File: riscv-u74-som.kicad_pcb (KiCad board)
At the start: 2 copper layers, 55 x 40 mm, 13 parts, among them J1 DF40HC(3.0)-100DS-0.4v, J2 DF40HC(3.0)-100DS-0.4v, U1 SiFive-U74, U2 MT53E256M32D2, U3 MT53E256M32D2, U4 S25FL128SAGNFI000, U5 TPS65086100, U6 TDA19988BHN_C1,557, U7 KSZ9031RNXCA

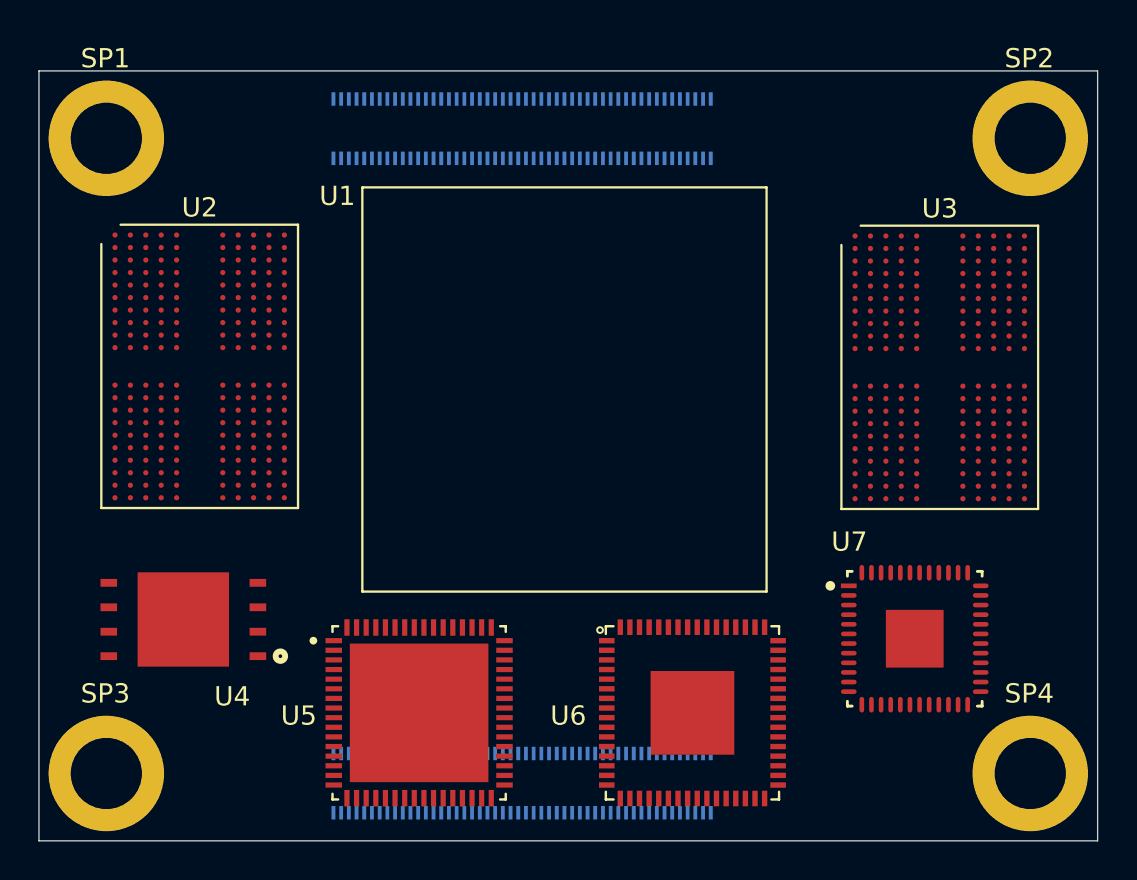
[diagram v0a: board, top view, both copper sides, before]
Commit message: Flipped standoffs in mock PCB
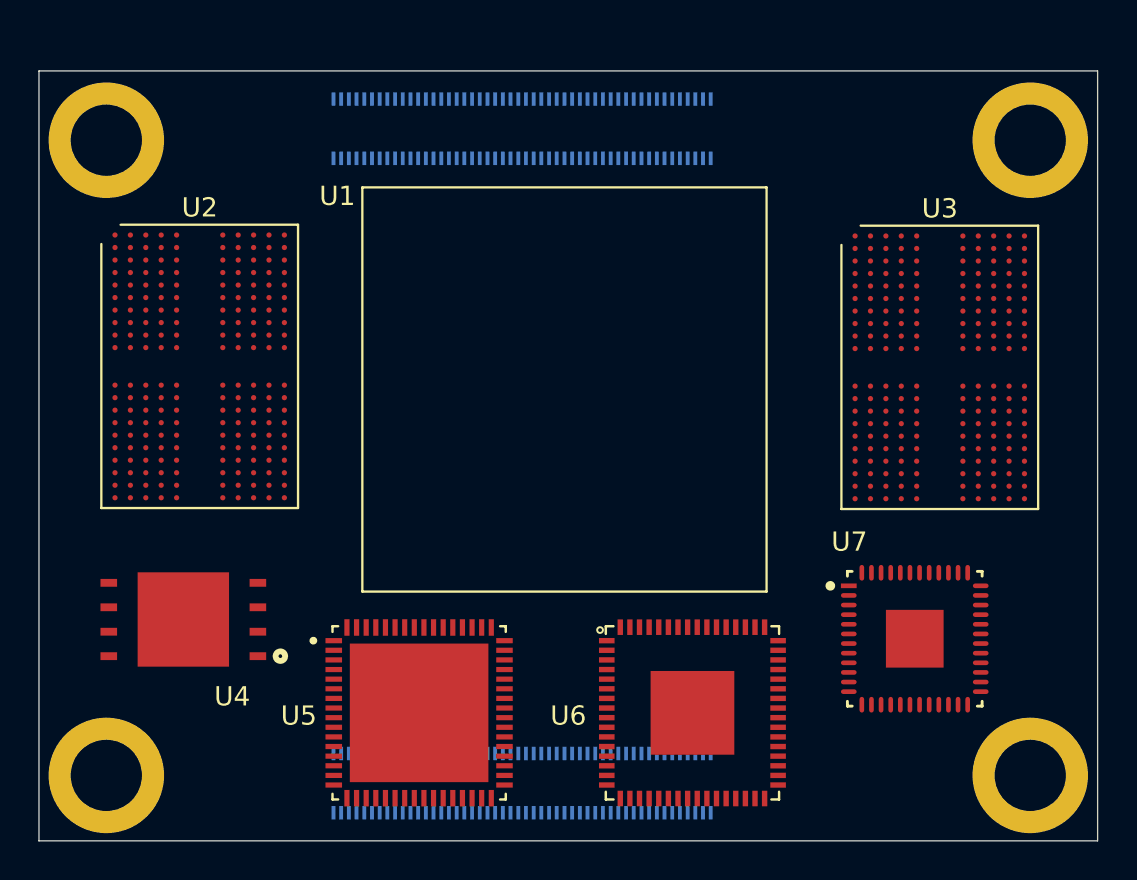
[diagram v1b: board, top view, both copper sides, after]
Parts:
- SP1, SP2, SP3, SP4: moved to B.Cu

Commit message: Updated mock
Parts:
- removed J1, J2: DF40HC(3.0)-100DS-0.4v, antmicro-footprints:DF40HC(3.0)-100DS-0.4v
- removed U1: SiFive-U74, antmicro-footprints:SiFive-U74
- removed U4: S25FL128SAGNFI000, antmicro-footprints:S25FL128SAGNFI000
- removed U5: TPS65086100, antmicro-footprints:QFN50P900X900X80-65N
- removed U6: TDA19988BHN_C1,557, antmicro-footprints:QFN50P900X900X100-65N
- removed U7: KSZ9031RNXCA, antmicro-footprints:QFN-48-Microchip-QFN77-48LD-PL-2
- added G***: LOGO, antmicro-footprints:antmicro-logo_scaled_15mm, F.Cu at (147.9, 58.2)
- added J3: DF40C-100DP-0.4V(51), antmicro-footprints:HRS_DF40C-100DP-0.4V(51), B.Cu at (155.1, 58.0)
- added J4: DF40C-100DP-0.4V(51), antmicro-footprints:HRS_DF40C-100DP-0.4V(51), B.Cu at (155.1, 92.0)
- added U10: TDA19988BHN_C1,557, antmicro-footprints:QFN50P900X900X100-65N, F.Cu at (164.0, 88.3)
- added U11: KSZ9031RNXCA, antmicro-footprints:QFN-48-Microchip-QFN77-48LD-PL-2, F.Cu at (173.0, 60.5)
- added U13: VIC7100, antmicro-footprints:vic7100, F.Cu at (145.3, 61.9)
- added U8: TPS65086100, antmicro-footprints:QFN50P900X900X80-65N, F.Cu at (146.8, 88.3)
- added U9: GD25LQ256DWIGR, antmicro-footprints:8-WSON-6x5, F.Cu at (177.0, 86.0)
- SP1, SP2, SP3, SP4: footprint antmicro-footprints:9774030151 -> riscv-u74-som-footprints:9774030151
- U2, U3: footprint antmicro-footprints:BGA-200_10.0x14.5mm_Layout12x22_P0.80x0.65mm -> riscv-u74-som-footprints:BGA-200_10.0x14.5mm_Layout12x22_P0.80x0.65mm
- moved U2 3.81 mm to (136.9, 73.8)
- moved U3 3.81 mm to (175.3, 73.9)
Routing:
- net (no net): track 0.00 -> 225.1 mm, vias 0 -> 20
- net Net-(U2-PadA10): track 0.00 -> 25.6 mm
- net GND: track 0.00 -> 19.7 mm, vias 0 -> 4
- net Net-(U3-PadAB10): track 0.00 -> 9.79 mm, vias 0 -> 1
- net Net-(U2-PadC11): track 0.00 -> 9.35 mm
- net Net-(U3-PadAA1): track 0.00 -> 9.35 mm
- net Net-(U2-PadA4): track 0.00 -> 8.92 mm
- net Net-(U13-PadAF1): track 0.00 -> 8.92 mm
- net USB_SSTXA2: track 0.00 -> 8.92 mm
- net RPI_GPIO8: track 0.00 -> 8.88 mm
- net DDR1_DQ05: track 0.00 -> 8.88 mm
- net RPI_GPIO20: track 0.00 -> 7.87 mm
- net DDR1_DQ02: track 0.00 -> 7.87 mm
- net CSI1RX_CLK_P: track 0.00 -> 7.15 mm
- net Net-(U13-PadAG1): track 0.00 -> 7.15 mm
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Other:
- net class Default: clearance 0.2 -> 0.1; trace_width 0.25 -> 0.11
- rule trace_clearance: 0.2 -> 0.1
- rule trace_min: 0.2 -> 0.11
- board text added: "ARV"
- board text added: "Rev. 1.0.0 04/2021"

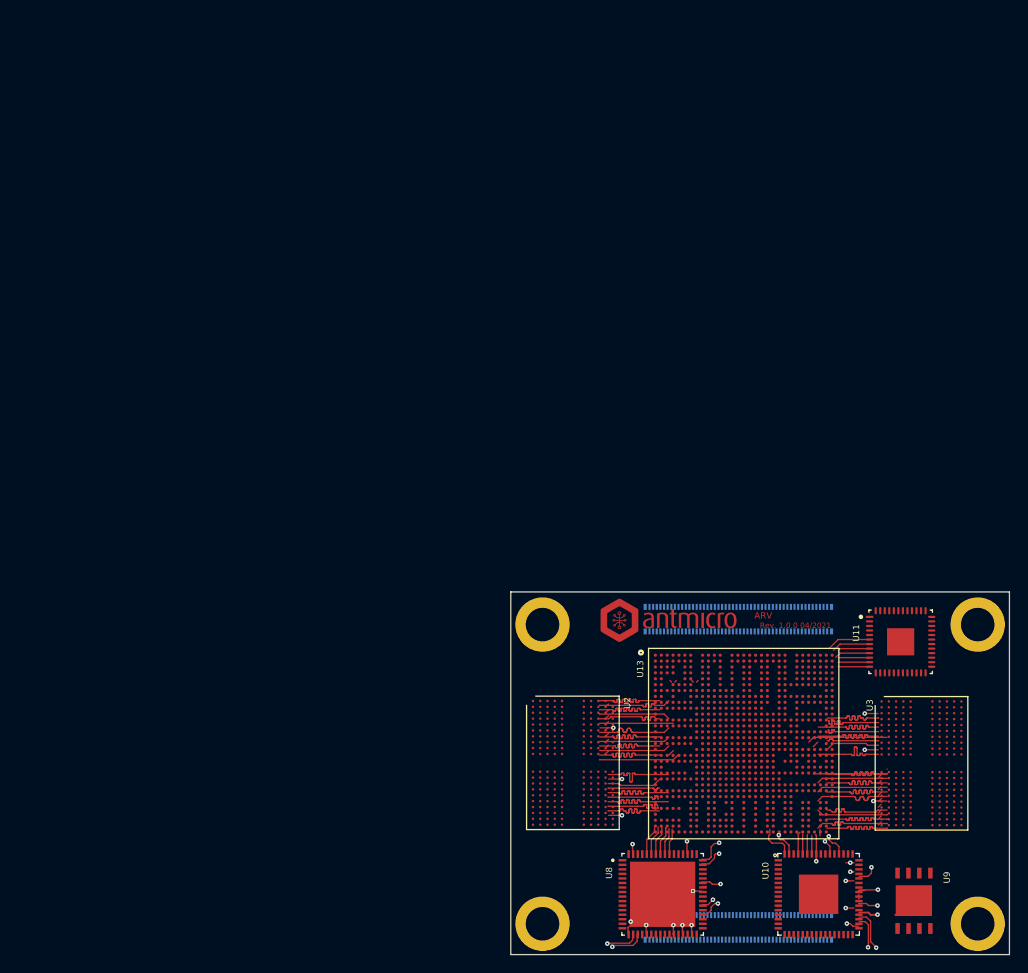
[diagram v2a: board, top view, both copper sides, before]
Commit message: Connected interfaces to VIC to visualise its ball locations (wip, mock purposes)
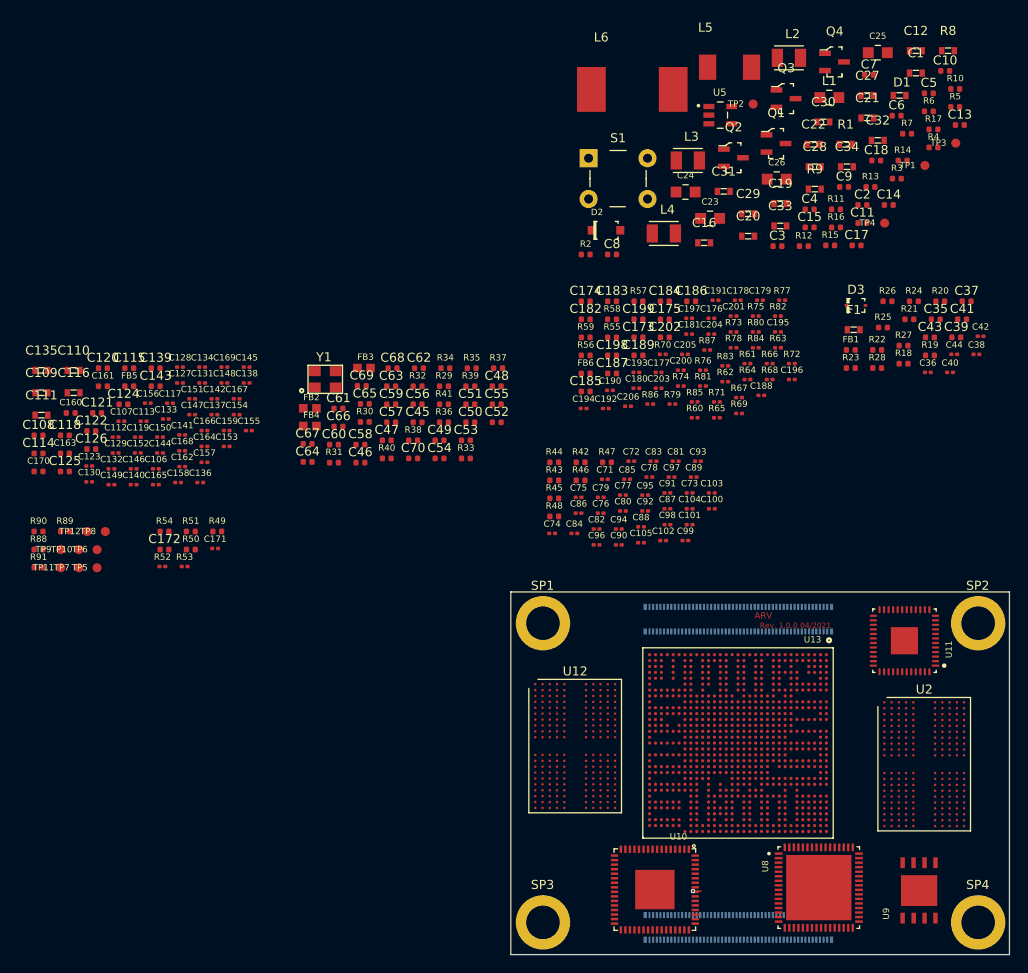
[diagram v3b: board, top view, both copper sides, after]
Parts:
- removed G***: LOGO, antmicro-footprints:antmicro-logo_scaled_15mm
- removed U3: MT53E256M32D2, riscv-u74-som-footprints:BGA-200_10.0x14.5mm_Layout12x22_P0.80x0.65mm
- added C1: C_10u_0603, antmicro-footprints:0603-cap, F.Cu at (174.7, -2.26)
- added C10: C_100n_0402_16V, antmicro-footprints:0402-cap, F.Cu at (177.9, -2.50)
- added C100: C_100n_0201, antmicro-footprints:0201-res, F.Cu at (152.2, 45.8)
- added C101: C_100n_0201, antmicro-footprints:0201-res, F.Cu at (149.7, 47.6)
- added C102: C_100n_0201, antmicro-footprints:0201-res, F.Cu at (146.8, 49.3)
- added C103: C_100n_0201, antmicro-footprints:0201-res, F.Cu at (152.2, 44.1)
- added C104: C_100n_0201, antmicro-footprints:0201-res, F.Cu at (149.7, 45.8)
- added C105: C_100n_0201, antmicro-footprints:0201-res, F.Cu at (144.4, 49.5)
- added C106: C_100n_0201, antmicro-footprints:0201-res, F.Cu at (90.9, 41.4)
- added C107: C_100n_0201, antmicro-footprints:0201-res, F.Cu at (87.1, 36.1)
- added C108: C_1u_0402, antmicro-footprints:0402-cap, F.Cu at (77.9, 37.7)
- added C109: C_22u_0603, antmicro-footprints:0603-cap, F.Cu at (78.3, 33.0)
- added C11: C_4u7_0402, antmicro-footprints:0402-cap, F.Cu at (168.8, 14.3)
- added C110: C_22u_0603, antmicro-footprints:0603-cap, F.Cu at (81.8, 30.5)
- added C111: C_22u_0603, antmicro-footprints:0603-cap, F.Cu at (78.3, 35.5)
- added C112: C_100n_0201, antmicro-footprints:0201-res, F.Cu at (86.4, 37.9)
- added C113: C_100n_0201, antmicro-footprints:0201-res, F.Cu at (89.5, 36.1)
- added C114: C_10u_0402, antmicro-footprints:0402-cap, F.Cu at (77.9, 39.7)
- added C115: C_10u_0402, antmicro-footprints:0402-cap, F.Cu at (87.9, 30.3)
- added C116: C_22u_0603, antmicro-footprints:0603-cap, F.Cu at (81.8, 33.0)
- added C117: C_100n_0201, antmicro-footprints:0201-res, F.Cu at (92.4, 34.2)
- added C118: C_10u_0402, antmicro-footprints:0402-cap, F.Cu at (80.8, 37.7)
- added C119: C_100n_0201, antmicro-footprints:0201-res, F.Cu at (88.9, 37.9)
- added C12: C_1n_0603, antmicro-footprints:0603-cap, F.Cu at (174.7, -4.73)
- added C120: C_10u_0402, antmicro-footprints:0402-cap, F.Cu at (85.0, 30.3)
- added C121: C_10u_0402, antmicro-footprints:0402-cap, F.Cu at (84.4, 35.2)
- added C122: C_10u_0402, antmicro-footprints:0402-cap, F.Cu at (83.8, 37.2)
- added C123: C_100n_0201, antmicro-footprints:0201-res, F.Cu at (83.5, 41.1)
- added C124: C_1u_0402, antmicro-footprints:0402-cap, F.Cu at (87.3, 34.3)
- added C125: C_1u_0402, antmicro-footprints:0402-cap, F.Cu at (80.8, 41.7)
- added C126: C_1u_0402, antmicro-footprints:0402-cap, F.Cu at (83.8, 39.2)
- added C127: C_100n_0201, antmicro-footprints:0201-res, F.Cu at (93.5, 31.9)
- added C128: C_100n_0201, antmicro-footprints:0201-res, F.Cu at (93.5, 30.2)
- added C129: C_100n_0201, antmicro-footprints:0201-res, F.Cu at (86.4, 39.6)
- added C13: C_100n_0402_16V, antmicro-footprints:0402-cap, F.Cu at (179.6, 3.47)
- added C130: C_100n_0201, antmicro-footprints:0201-res, F.Cu at (83.5, 42.8)
- added C131: C_100n_0201, antmicro-footprints:0201-res, F.Cu at (96.0, 31.9)
- added C132: C_100n_0201, antmicro-footprints:0201-res, F.Cu at (86.0, 41.4)
- added C133: C_100n_0201, antmicro-footprints:0201-res, F.Cu at (92.0, 35.9)
- added C134: C_100n_0201, antmicro-footprints:0201-res, F.Cu at (96.0, 30.2)
- added C135: C_22u_0603, antmicro-footprints:0603-cap, F.Cu at (78.3, 30.5)
- added C136: C_100n_0201, antmicro-footprints:0201-res, F.Cu at (95.8, 42.9)
- added C137: C_100n_0201, antmicro-footprints:0201-res, F.Cu at (97.3, 35.4)
- added C138: C_100n_0201, antmicro-footprints:0201-res, F.Cu at (100.9, 31.9)
- added C139: C_10u_0402, antmicro-footprints:0402-cap, F.Cu at (90.9, 30.3)
- added C14: C_4u7_0402, antmicro-footprints:0402-cap, F.Cu at (171.7, 12.3)
- added C140: C_100n_0201, antmicro-footprints:0201-res, F.Cu at (88.4, 43.1)
- added C141: C_100n_0201, antmicro-footprints:0201-res, F.Cu at (93.8, 37.7)
- added C142: C_100n_0201, antmicro-footprints:0201-res, F.Cu at (97.3, 33.7)
- added C143: C_1u_0402, antmicro-footprints:0402-cap, F.Cu at (90.9, 32.3)
- added C144: C_100n_0201, antmicro-footprints:0201-res, F.Cu at (91.3, 39.6)
- added C145: C_100n_0201, antmicro-footprints:0201-res, F.Cu at (100.9, 30.2)
- added C146: C_100n_0201, antmicro-footprints:0201-res, F.Cu at (88.4, 41.4)
- added C147: C_100n_0201, antmicro-footprints:0201-res, F.Cu at (94.9, 35.4)
- added C148: C_100n_0201, antmicro-footprints:0201-res, F.Cu at (98.4, 31.9)
- added C149: C_100n_0201, antmicro-footprints:0201-res, F.Cu at (86.0, 43.1)
- added C15: C_2u2_0402, antmicro-footprints:0402-cap, F.Cu at (163.0, 14.8)
- added C150: C_100n_0201, antmicro-footprints:0201-res, F.Cu at (91.3, 37.9)
- added C151: C_100n_0201, antmicro-footprints:0201-res, F.Cu at (94.9, 33.7)
- added C152: C_100n_0201, antmicro-footprints:0201-res, F.Cu at (88.9, 39.6)
- added C153: C_100n_0201, antmicro-footprints:0201-res, F.Cu at (98.7, 38.9)
- added C154: C_100n_0201, antmicro-footprints:0201-res, F.Cu at (99.8, 35.4)
- added C155: C_100n_0201, antmicro-footprints:0201-res, F.Cu at (101.1, 37.2)
- added C156: C_100n_0201, antmicro-footprints:0201-res, F.Cu at (90.0, 34.2)
- added C157: C_100n_0201, antmicro-footprints:0201-res, F.Cu at (96.2, 40.7)
- added C158: C_100n_0201, antmicro-footprints:0201-res, F.Cu at (93.3, 42.9)
- added C159: C_100n_0201, antmicro-footprints:0201-res, F.Cu at (98.7, 37.2)
- added C16: C_10u_0603, antmicro-footprints:0603-cap, F.Cu at (151.4, 16.5)
- added C160: C_1n_0402, antmicro-footprints:0402-res, F.Cu at (81.5, 35.2)
- added C161: C_1n_0402, antmicro-footprints:0402-res, F.Cu at (85.0, 32.3)
- added C162: C_100n_0201, antmicro-footprints:0201-res, F.Cu at (93.8, 41.2)
- added C163: C_1n_0402, antmicro-footprints:0402-res, F.Cu at (80.8, 39.7)
- added C164: C_100n_0201, antmicro-footprints:0201-res, F.Cu at (96.2, 38.9)
- added C165: C_100n_0201, antmicro-footprints:0201-res, F.Cu at (90.9, 43.1)
- added C166: C_100n_0201, antmicro-footprints:0201-res, F.Cu at (96.2, 37.2)
- added C167: C_100n_0201, antmicro-footprints:0201-res, F.Cu at (99.8, 33.7)
- added C168: C_100n_0201, antmicro-footprints:0201-res, F.Cu at (93.8, 39.4)
- added C169: C_100n_0201, antmicro-footprints:0201-res, F.Cu at (98.4, 30.2)
- added C17: C_100n_0402_16V, antmicro-footprints:0402-cap, F.Cu at (168.2, 16.8)
- added C170: C_1n_0402, antmicro-footprints:0402-res, F.Cu at (77.9, 41.7)
- added C171: C_100n_0201, antmicro-footprints:0201-res, F.Cu at (97.4, 50.2)
- added C172: C_10n_0402, antmicro-footprints:0402-cap, F.Cu at (91.8, 50.3)
- added C173: C_1u_0402, antmicro-footprints:0402-cap, F.Cu at (144.1, 26.9)
- added C174: C_1u_0402, antmicro-footprints:0402-cap, F.Cu at (138.3, 22.9)
- added C175: C_1u_0402, antmicro-footprints:0402-cap, F.Cu at (147.0, 24.9)
- added C176: C_100n_0201, antmicro-footprints:0201-res, F.Cu at (152.1, 24.8)
- added C177: C_100n_0201, antmicro-footprints:0201-res, F.Cu at (146.3, 30.8)
- added C178: C_100n_0201, antmicro-footprints:0201-res, F.Cu at (155.1, 22.8)
- added C179: C_100n_0201, antmicro-footprints:0201-res, F.Cu at (157.5, 22.8)
- added C18: C_100n_0402_16V, antmicro-footprints:0402-cap, F.Cu at (170.3, 7.39)
- added C180: C_100n_0201, antmicro-footprints:0201-res, F.Cu at (143.9, 32.5)
- added C181: C_100n_0201, antmicro-footprints:0201-res, F.Cu at (149.7, 26.5)
- added C182: C_10u_0402, antmicro-footprints:0402-cap, F.Cu at (138.3, 24.9)
- added C183: C_1u_0402, antmicro-footprints:0402-cap, F.Cu at (141.2, 22.9)
- added C184: C_10u_0402, antmicro-footprints:0402-cap, F.Cu at (147.0, 22.9)
- added C185: C_1u_0402, antmicro-footprints:0402-cap, F.Cu at (138.3, 32.9)
- added C186: C_1u_0402, antmicro-footprints:0402-cap, F.Cu at (149.9, 22.9)
- added C187: C_1u_0402, antmicro-footprints:0402-cap, F.Cu at (141.2, 30.9)
- added C188: C_100n_0201, antmicro-footprints:0201-res, F.Cu at (157.7, 33.3)
- added C189: C_1u_0402, antmicro-footprints:0402-cap, F.Cu at (144.1, 28.9)
- added C19: C_22u_0603, antmicro-footprints:0603-cap, F.Cu at (159.8, 12.1)
- added C190: C_100n_0201, antmicro-footprints:0201-res, F.Cu at (141.0, 32.7)
- added C191: C_100n_0201, antmicro-footprints:0201-res, F.Cu at (152.6, 22.8)
- added C192: C_100n_0201, antmicro-footprints:0201-res, F.Cu at (140.5, 34.7)
- added C193: C_100n_0201, antmicro-footprints:0201-res, F.Cu at (143.9, 30.8)
- added C194: C_100n_0201, antmicro-footprints:0201-res, F.Cu at (138.1, 34.7)
- added C195: C_100n_0201, antmicro-footprints:0201-res, F.Cu at (159.5, 26.3)
- added C196: C_100n_0201, antmicro-footprints:0201-res, F.Cu at (161.0, 31.5)
- added C197: C_100n_0201, antmicro-footprints:0201-res, F.Cu at (149.7, 24.8)
- added C198: C_1u_0402, antmicro-footprints:0402-cap, F.Cu at (141.2, 28.9)
- added C199: C_1u_0402, antmicro-footprints:0402-cap, F.Cu at (144.1, 24.9)
- added C2: C_2u2_0402, antmicro-footprints:0402-cap, F.Cu at (168.8, 12.3)
- added C20: C_22u_0603, antmicro-footprints:0603-cap, F.Cu at (156.2, 15.7)
- added C200: C_100n_0201, antmicro-footprints:0201-res, F.Cu at (148.8, 30.5)
- added C201: C_100n_0201, antmicro-footprints:0201-res, F.Cu at (154.6, 24.5)
- added C202: C_1u_0402, antmicro-footprints:0402-cap, F.Cu at (147.0, 26.9)
- added C203: C_100n_0201, antmicro-footprints:0201-res, F.Cu at (146.3, 32.5)
- added C204: C_100n_0201, antmicro-footprints:0201-res, F.Cu at (152.1, 26.5)
- added C205: C_100n_0201, antmicro-footprints:0201-res, F.Cu at (149.2, 28.8)
- added C206: C_100n_0201, antmicro-footprints:0201-res, F.Cu at (143.0, 34.5)
- added C21: C_22u_0603, antmicro-footprints:0603-cap, F.Cu at (169.4, 2.69)
- added C22: C_22u_0603, antmicro-footprints:0603-cap, F.Cu at (163.4, 5.60)
- added C23: C_100u_0805, antmicro-footprints:0805-cap, F.Cu at (152.0, 13.8)
- added C24: C_100u_0805, antmicro-footprints:0805-cap, F.Cu at (149.3, 10.9)
- added C25: C_100u_0805, antmicro-footprints:0805-cap, F.Cu at (170.5, -4.51)
- added C26: C_100u_0805, antmicro-footprints:0805-cap, F.Cu at (159.4, 9.44)
- added C27: C_10u_0603, antmicro-footprints:0603-cap, F.Cu at (169.4, 0.22)
- added C28: C_10u_0603, antmicro-footprints:0603-cap, F.Cu at (163.6, 8.07)
- added C29: C_22u_0603, antmicro-footprints:0603-cap, F.Cu at (156.2, 13.3)
- added C3: C_2u2_0402, antmicro-footprints:0402-cap, F.Cu at (159.4, 16.8)
- added C30: C_22u_0603, antmicro-footprints:0603-cap, F.Cu at (164.5, 3.13)
- added C31: C_22u_0603, antmicro-footprints:0603-cap, F.Cu at (153.5, 10.8)
- added C32: C_22u_0603, antmicro-footprints:0603-cap, F.Cu at (170.5, 5.16)
- added C33: C_22u_0603, antmicro-footprints:0603-cap, F.Cu at (159.8, 14.6)
- added C34: C_22u_0603, antmicro-footprints:0603-cap, F.Cu at (167.1, 8.07)
- added C35: C_1u_0402, antmicro-footprints:0402-cap, F.Cu at (176.9, 24.9)
- added C36: C_100n_0201, antmicro-footprints:0201-res, F.Cu at (176.0, 30.8)
- added C37: C_2u2_0402, antmicro-footprints:0402-cap, F.Cu at (180.3, 22.9)
- added C38: C_100n_0201, antmicro-footprints:0201-res, F.Cu at (181.4, 28.8)
- added C39: C_2u2_0402, antmicro-footprints:0402-cap, F.Cu at (179.2, 26.9)
- added C4: C_2u2_0402, antmicro-footprints:0402-cap, F.Cu at (163.0, 12.8)
- added C40: C_100n_0201, antmicro-footprints:0201-res, F.Cu at (178.5, 30.8)
- added C41: C_2u2_0402, antmicro-footprints:0402-cap, F.Cu at (179.8, 24.9)
- added C42: C_100n_0201, antmicro-footprints:0201-res, F.Cu at (181.8, 26.8)
- added C43: C_2u2_0402, antmicro-footprints:0402-cap, F.Cu at (176.3, 26.9)
- added C44: C_100n_0201, antmicro-footprints:0201-res, F.Cu at (178.9, 28.8)
- added C45: C_4u7_0402, antmicro-footprints:0402-cap, F.Cu at (119.7, 36.3)
- added C46: C_470n_0402, antmicro-footprints:0402-cap, F.Cu at (113.4, 40.7)
- added C47: C_4u7_0402, antmicro-footprints:0402-cap, F.Cu at (116.3, 38.3)
- added C48: C_470n_0402, antmicro-footprints:0402-cap, F.Cu at (128.5, 32.3)
- added C49: C_4u7_0402, antmicro-footprints:0402-cap, F.Cu at (122.2, 38.3)
- added C5: C_2u2_0402, antmicro-footprints:0402-cap, F.Cu at (176.1, -0.03)
- added C50: C_4u7_0402, antmicro-footprints:0402-cap, F.Cu at (125.6, 36.3)
- added C51: C_470n_0402, antmicro-footprints:0402-cap, F.Cu at (125.6, 34.3)
- added C52: C_470n_0402, antmicro-footprints:0402-cap, F.Cu at (128.5, 36.3)
- added C53: C_470n_0402, antmicro-footprints:0402-cap, F.Cu at (125.1, 38.3)
- added C54: C_100n_0402, antmicro-footprints:0402-cap, F.Cu at (122.2, 40.2)
- added C55: C_10n_0402, antmicro-footprints:0402-cap, F.Cu at (128.5, 34.3)
- added C56: C_10n_0402, antmicro-footprints:0402-cap, F.Cu at (119.7, 34.3)
- added C57: C_10n_0402, antmicro-footprints:0402-cap, F.Cu at (116.8, 36.3)
- added C58: C_4u7_0402, antmicro-footprints:0402-cap, F.Cu at (113.4, 38.7)
- added C59: C_10n_0402, antmicro-footprints:0402-cap, F.Cu at (116.8, 34.3)
- added C6: C_4u7_0402, antmicro-footprints:0402-cap, F.Cu at (172.6, 2.44)
- added C60: C_10n_0402, antmicro-footprints:0402-cap, F.Cu at (110.5, 38.7)
- added C61: C_10n_0402, antmicro-footprints:0402-cap, F.Cu at (111.0, 34.7)
- added C62: C_10n_0402, antmicro-footprints:0402-cap, F.Cu at (119.9, 30.3)
- added C63: C_10n_0402, antmicro-footprints:0402-cap, F.Cu at (116.8, 32.3)
- added C64: C_10n_0402, antmicro-footprints:0402-cap, F.Cu at (107.6, 40.6)
- added C65: C_10n_0402, antmicro-footprints:0402-cap, F.Cu at (113.9, 34.2)
- added C66: C_10n_0402, antmicro-footprints:0402-cap, F.Cu at (111.0, 36.7)
- added C67: C_10n_0402, antmicro-footprints:0402-cap, F.Cu at (107.6, 38.6)
- added C68: C_10n_0402, antmicro-footprints:0402-cap, F.Cu at (117.0, 30.3)
- added C69: C_22p_0402, antmicro-footprints:0402-cap, F.Cu at (113.6, 32.2)
- added C7: C_2u2_0402, antmicro-footprints:0402-cap, F.Cu at (169.5, -2.06)
- added C70: C_22p_0402, antmicro-footprints:0402-cap, F.Cu at (119.3, 40.2)
- added C71: C_100n_0201, antmicro-footprints:0201-res, F.Cu at (140.4, 42.5)
- added C72: C_100n_0201, antmicro-footprints:0201-res, F.Cu at (143.3, 40.6)
- added C73: C_100n_0201, antmicro-footprints:0201-res, F.Cu at (149.7, 44.1)
- added C74: C_100n_0201, antmicro-footprints:0201-res, F.Cu at (134.6, 48.5)
- added C75: C_100n_0201, antmicro-footprints:0201-res, F.Cu at (137.5, 44.5)
- added C76: C_100n_0201, antmicro-footprints:0201-res, F.Cu at (139.9, 46.3)
- added C77: C_100n_0201, antmicro-footprints:0201-res, F.Cu at (142.4, 44.3)
- added C78: C_100n_0201, antmicro-footprints:0201-res, F.Cu at (145.3, 42.3)
- added C79: C_100n_0201, antmicro-footprints:0201-res, F.Cu at (139.9, 44.5)
- added C8: C_2u2_0402, antmicro-footprints:0402-cap, F.Cu at (141.2, 17.8)
- added C80: C_100n_0201, antmicro-footprints:0201-res, F.Cu at (142.4, 46.0)
- added C81: C_100n_0201, antmicro-footprints:0201-res, F.Cu at (148.2, 40.6)
- added C82: C_100n_0201, antmicro-footprints:0201-res, F.Cu at (139.5, 48.0)
- added C83: C_100n_0201, antmicro-footprints:0201-res, F.Cu at (145.8, 40.6)
- added C84: C_100n_0201, antmicro-footprints:0201-res, F.Cu at (137.0, 48.5)
- added C85: C_100n_0201, antmicro-footprints:0201-res, F.Cu at (142.9, 42.5)
- added C86: C_100n_0201, antmicro-footprints:0201-res, F.Cu at (137.5, 46.3)
- added C87: C_100n_0201, antmicro-footprints:0201-res, F.Cu at (147.3, 45.8)
- added C88: C_100n_0201, antmicro-footprints:0201-res, F.Cu at (144.4, 47.8)
- added C89: C_100n_0201, antmicro-footprints:0201-res, F.Cu at (150.2, 42.3)
- added C9: C_2u2_0402, antmicro-footprints:0402-cap, F.Cu at (166.8, 10.3)
- added C90: C_100n_0201, antmicro-footprints:0201-res, F.Cu at (141.9, 49.8)
- added C91: C_100n_0201, antmicro-footprints:0201-res, F.Cu at (147.3, 44.1)
- added C92: C_100n_0201, antmicro-footprints:0201-res, F.Cu at (144.8, 46.0)
- added C93: C_100n_0201, antmicro-footprints:0201-res, F.Cu at (150.7, 40.6)
- added C94: C_100n_0201, antmicro-footprints:0201-res, F.Cu at (141.9, 48.0)
- added C95: C_100n_0201, antmicro-footprints:0201-res, F.Cu at (144.8, 44.3)
- added C96: C_100n_0201, antmicro-footprints:0201-res, F.Cu at (139.5, 49.8)
- added C97: C_100n_0201, antmicro-footprints:0201-res, F.Cu at (147.8, 42.3)
- added C98: C_100n_0201, antmicro-footprints:0201-res, F.Cu at (147.3, 47.6)
- added C99: C_100n_0201, antmicro-footprints:0201-res, F.Cu at (149.3, 49.3)
- added D1: PGB1010603MR, antmicro-footprints:PGB1010603MR, F.Cu at (172.9, 0.21)
- added D2: 1N4148W-TP, antmicro-footprints:SOD-123, F.Cu at (140.5, 15.1)
- added D3: 1N4148WS, antmicro-footprints:SOD-323F, F.Cu at (168.1, 23.4)
- added F1: 0ZCM0002FF2G, antmicro-footprints:0603-res, F.Cu at (167.8, 26.1)
- added FB1: BLM15PD121SN1D, antmicro-footprints:0402-res, F.Cu at (167.5, 28.3)
- added FB2: BLM18AG601SN1D, antmicro-footprints:0603, F.Cu at (107.9, 34.7)
- added FB3: BLM18AG601SN1D, antmicro-footprints:0603, F.Cu at (113.8, 30.3)
- added FB4: BLM18AG601SN1D, antmicro-footprints:0603, F.Cu at (107.9, 36.7)
- added FB5: BLM15PD121SN1D, antmicro-footprints:0402-res, F.Cu at (87.9, 32.3)
- added FB6: BLM15PD121SN1D, antmicro-footprints:0402-res, F.Cu at (138.3, 30.9)
- added L1: 10uH, antmicro-footprints:0805-res, F.Cu at (165.2, 0.44)
- added L2: LQH32PN1R0NN0L, antmicro-footprints:IND_LQH32PN1R0NN0L, F.Cu at (160.7, -3.94)
- added L3: LQH32PN1R0NN0L, antmicro-footprints:IND_LQH32PN1R0NN0L, F.Cu at (149.6, 7.38)
- added L4: LQH32PN1R0NN0L, antmicro-footprints:IND_LQH32PN1R0NN0L, F.Cu at (146.9, 15.4)
- added L5: MPX1D0520LR47, antmicro-footprints:MPX1D0520LR47, F.Cu at (150.8, -4.30)
- added L6: IHLP4040DZERR56M01, antmicro-footprints:IHLP4040DZERR56M01, F.Cu at (138.0, -1.90)
- added Q1: BSS138AKA, antmicro-footprints:SOT-23-3, F.Cu at (159.3, 5.51)
- added Q2: BSS138AKA, antmicro-footprints:SOT-23-3, F.Cu at (154.6, 7.08)
- added Q3: BSS138AKA, antmicro-footprints:SOT-23-3, F.Cu at (160.4, 0.56)
- added Q4: BSS138AKA, antmicro-footprints:SOT-23-3, F.Cu at (165.7, -3.49)
- added R1: R_1M_0603, antmicro-footprints:0603-res, F.Cu at (167.0, 5.60)
- added R10: R_0R_0402, antmicro-footprints:0402-res, F.Cu at (179.0, -0.51)
- added R11: R_0R_0402, antmicro-footprints:0402-res, F.Cu at (165.9, 12.8)
- added R12: R_0R_0402, antmicro-footprints:0402-res, F.Cu at (162.3, 16.8)
- added R13: R_4k7_0402, antmicro-footprints:0402-res, F.Cu at (169.7, 10.3)
- added R14: R_0R_0402, antmicro-footprints:0402-res, F.Cu at (173.2, 7.39)
- added R15: R_0R_0402, antmicro-footprints:0402-res, F.Cu at (165.3, 16.8)
- added R16: R_0R_0402, antmicro-footprints:0402-res, F.Cu at (165.9, 14.8)
- added R17: R_4k7_0402, antmicro-footprints:0402-res, F.Cu at (176.6, 3.95)
- added R18: R_33R_0402, antmicro-footprints:0402-res, F.Cu at (173.3, 29.8)
- added R19: R_33R_0402, antmicro-footprints:0402-res, F.Cu at (176.3, 28.9)
- added R2: R_10k_0402, antmicro-footprints:0402-res, F.Cu at (138.3, 17.8)
- added R20: R_33R_0402, antmicro-footprints:0402-res, F.Cu at (177.4, 22.9)
- added R21: R_4k7_0402, antmicro-footprints:0402-res, F.Cu at (174.0, 24.9)
- added R22: R_33R_0402, antmicro-footprints:0402-res, F.Cu at (170.4, 28.3)
- added R23: R_33R_0402, antmicro-footprints:0402-res, F.Cu at (167.5, 30.3)
- added R24: R_33R_0402, antmicro-footprints:0402-res, F.Cu at (174.5, 22.9)
- added R25: R_10k_0402, antmicro-footprints:0402-res, F.Cu at (171.1, 25.8)
- added R26: R_1k_0402, antmicro-footprints:0402-res, F.Cu at (171.6, 22.9)
- added R27: R_1k_0402, antmicro-footprints:0402-res, F.Cu at (173.3, 27.8)
- added R28: R_27k_0402, antmicro-footprints:0402-res, F.Cu at (170.4, 30.3)
- added R29: R_1k_0402, antmicro-footprints:0402-res, F.Cu at (122.7, 32.3)
- added R3: R_10k_0402, antmicro-footprints:0402-res, F.Cu at (172.6, 9.38)
- added R30: R_12k1_0402, antmicro-footprints:0402-res, F.Cu at (113.9, 36.2)
- added R31: R_10k_0402, antmicro-footprints:0402-res, F.Cu at (110.5, 40.7)
- added R32: R_10k_0402, antmicro-footprints:0402-res, F.Cu at (119.7, 32.3)
- added R33: R_10k_0402, antmicro-footprints:0402-res, F.Cu at (125.1, 40.2)
- added R34: R_10k_0402, antmicro-footprints:0402-res, F.Cu at (122.8, 30.3)
- added R35: R_10k_0402, antmicro-footprints:0402-res, F.Cu at (125.7, 30.3)
- added R36: R_10k_0402, antmicro-footprints:0402-res, F.Cu at (122.7, 36.3)
- added R37: R_4k7_0402, antmicro-footprints:0402-res, F.Cu at (128.6, 30.3)
- added R38: R_10k_0402, antmicro-footprints:0402-res, F.Cu at (119.3, 38.3)
- added R39: R_10k_0402, antmicro-footprints:0402-res, F.Cu at (125.6, 32.3)
- added R4: R_10k_0402, antmicro-footprints:0402-res, F.Cu at (176.6, 5.94)
- added R40: R_10k_0402, antmicro-footprints:0402-res, F.Cu at (116.3, 40.2)
- added R41: R_1M5_0402, antmicro-footprints:0402-res, F.Cu at (122.7, 34.3)
- added R42: R_10k_0402, antmicro-footprints:0402-res, F.Cu at (137.7, 40.7)
- added R43: R_10k_0402, antmicro-footprints:0402-res, F.Cu at (134.8, 42.7)
- added R44: R_10k_0402, antmicro-footprints:0402-res, F.Cu at (134.8, 40.7)
- added R45: R_240R_0402, antmicro-footprints:0402-res, F.Cu at (134.8, 44.7)
- added R46: R_0R_0402, antmicro-footprints:0402-res, F.Cu at (137.7, 42.7)
- added R47: R_10k_0402, antmicro-footprints:0402-res, F.Cu at (140.6, 40.7)
- added R48: R_0R_0402, antmicro-footprints:0402-res, F.Cu at (134.8, 46.6)
- added R49: R_10k_0402, antmicro-footprints:0402-res, F.Cu at (97.6, 48.3)
- added R5: R_0R_0402, antmicro-footprints:0402-res, F.Cu at (179.0, 1.48)
- added R50: R_10k_0402, antmicro-footprints:0402-res, F.Cu at (94.7, 50.3)
- added R51: R_10k_0402, antmicro-footprints:0402-res, F.Cu at (94.7, 48.3)
- added R52: R_0R_0201, antmicro-footprints:0201-res, F.Cu at (91.6, 52.2)
- added R53: R_0R_0201, antmicro-footprints:0201-res, F.Cu at (94.0, 52.2)
- added R54: R_10k_0402, antmicro-footprints:0402-res, F.Cu at (91.8, 48.3)
- added R55: R_33R_0402, antmicro-footprints:0402-res, F.Cu at (141.2, 26.9)
- added R56: R_33R_0402, antmicro-footprints:0402-res, F.Cu at (138.3, 28.9)
- added R57: R_33R_0402, antmicro-footprints:0402-res, F.Cu at (144.1, 22.9)
- added R58: R_33R_0402, antmicro-footprints:0402-res, F.Cu at (141.2, 24.9)
- added R59: R_33R_0402, antmicro-footprints:0402-res, F.Cu at (138.3, 26.9)
- added R6: R_0R_0402, antmicro-footprints:0402-res, F.Cu at (176.1, 1.96)
- added R60: R_33R_0201, antmicro-footprints:0201-res, F.Cu at (150.3, 35.8)
- added R61: R_33R_0201, antmicro-footprints:0201-res, F.Cu at (156.1, 29.8)
- added R62: R_33R_0201, antmicro-footprints:0201-res, F.Cu at (153.7, 31.8)
- added R63: R_33R_0201, antmicro-footprints:0201-res, F.Cu at (159.5, 28.0)
- added R64: R_33R_0201, antmicro-footprints:0201-res, F.Cu at (156.1, 31.5)
- added R65: R_33R_0201, antmicro-footprints:0201-res, F.Cu at (152.8, 35.8)
- added R66: R_33R_0201, antmicro-footprints:0201-res, F.Cu at (158.6, 29.8)
- added R67: R_33R_0201, antmicro-footprints:0201-res, F.Cu at (155.2, 33.5)
- added R68: R_33R_0201, antmicro-footprints:0201-res, F.Cu at (158.6, 31.5)
- added R69: R_33R_0201, antmicro-footprints:0201-res, F.Cu at (155.2, 35.3)
- added R7: R_2k2_0402, antmicro-footprints:0402-res, F.Cu at (173.7, 4.43)
- added R70: R_33R_0201, antmicro-footprints:0201-res, F.Cu at (146.8, 28.8)
- added R71: R_33R_0201, antmicro-footprints:0201-res, F.Cu at (152.8, 34.0)
- added R72: R_33R_0201, antmicro-footprints:0201-res, F.Cu at (161.0, 29.8)
- added R73: R_33R_0201, antmicro-footprints:0201-res, F.Cu at (154.6, 26.3)
- added R74: R_33R_0201, antmicro-footprints:0201-res, F.Cu at (148.8, 32.3)
- added R75: R_33R_0201, antmicro-footprints:0201-res, F.Cu at (157.0, 24.5)
- added R76: R_33R_0201, antmicro-footprints:0201-res, F.Cu at (151.2, 30.5)
- added R77: R_33R_0201, antmicro-footprints:0201-res, F.Cu at (160.0, 22.8)
- added R78: R_33R_0201, antmicro-footprints:0201-res, F.Cu at (154.6, 28.0)
- added R79: R_33R_0201, antmicro-footprints:0201-res, F.Cu at (147.9, 34.3)
- added R8: R_549k_0603, antmicro-footprints:0603-res, F.Cu at (178.3, -4.73)
- added R80: R_33R_0201, antmicro-footprints:0201-res, F.Cu at (157.0, 26.3)
- added R81: R_33R_0201, antmicro-footprints:0201-res, F.Cu at (151.2, 32.3)
- added R82: R_33R_0201, antmicro-footprints:0201-res, F.Cu at (159.5, 24.5)
- added R83: R_33R_0201, antmicro-footprints:0201-res, F.Cu at (153.7, 30.0)
- added R84: R_33R_0201, antmicro-footprints:0201-res, F.Cu at (157.0, 28.0)
- added R85: R_33R_0201, antmicro-footprints:0201-res, F.Cu at (150.3, 34.0)
- added R86: R_33R_0201, antmicro-footprints:0201-res, F.Cu at (145.4, 34.3)
- added R87: R_33R_0201, antmicro-footprints:0201-res, F.Cu at (151.7, 28.3)
- added R88: R_10k_0402, antmicro-footprints:0402-res, F.Cu at (77.9, 50.3)
- added R89: R_240R_0402, antmicro-footprints:0402-res, F.Cu at (80.8, 48.3)
- added R9: R_13k3_0603, antmicro-footprints:0603-res, F.Cu at (163.6, 10.5)
- added R90: R_10k_0402, antmicro-footprints:0402-res, F.Cu at (77.9, 48.3)
- added R91: R_240R_0402, antmicro-footprints:0402-res, F.Cu at (77.9, 52.3)
- added S1: B3F-1000, antmicro-footprints:Switch_Tactile_THT_B3F-1xxx, F.Cu at (138.6, 7.12)
- added TP1: TP_SMD1MM, antmicro-footprints:Testpoint_smd_1mm, F.Cu at (175.7, 7.99)
- added TP10: TP_SMD1MM, antmicro-footprints:Testpoint_smd_1mm, F.Cu at (82.4, 50.4)
- added TP11: TP_SMD1MM, antmicro-footprints:Testpoint_smd_1mm, F.Cu at (80.4, 52.3)
- added TP12: TP_SMD1MM, antmicro-footprints:Testpoint_smd_1mm, F.Cu at (83.3, 48.4)
- added TP2: TP_SMD1MM, antmicro-footprints:Testpoint_smd_1mm, F.Cu at (156.8, 1.21)
- added TP3: TP_SMD1MM, antmicro-footprints:Testpoint_smd_1mm, F.Cu at (179.1, 5.52)
- added TP4: TP_SMD1MM, antmicro-footprints:Testpoint_smd_1mm, F.Cu at (171.3, 14.3)
- added TP5: TP_SMD1MM, antmicro-footprints:Testpoint_smd_1mm, F.Cu at (84.4, 52.4)
- added TP6: TP_SMD1MM, antmicro-footprints:Testpoint_smd_1mm, F.Cu at (84.4, 50.4)
- added TP7: TP_SMD1MM, antmicro-footprints:Testpoint_smd_1mm, F.Cu at (82.4, 52.4)
- added TP8: TP_SMD1MM, antmicro-footprints:Testpoint_smd_1mm, F.Cu at (85.3, 48.4)
- added TP9: TP_SMD1MM, antmicro-footprints:Testpoint_smd_1mm, F.Cu at (80.4, 50.3)
- added U12: MT53E256M32D2DS-053, antmicro-footprints:BGA-200_10.0x14.5mm_Layout12x22_P0.80x0.65mm, F.Cu at (137.1, 72.0)
- added U5: LMR62014XMF_NOPB, antmicro-footprints:SOT95P280X145-5N, F.Cu at (153.1, 2.38)
- added Y1: ABM8G-25.000MHZ-18-D2Y-T, antmicro-footprints:KX-7, F.Cu at (109.5, 31.5)
- SP1, SP2, SP3, SP4: moved to F.Cu
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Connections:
- J3 pad 10: TRD0_N -> ETH0_N
- J3 pad 11: TRD2_P -> ETH2_P
- J3 pad 12: TRD0_P -> ETH0_P
- J3 pad 15: ETH_LEDG -> ETH_LED2
- J3 pad 17: ETH_LEDY -> ETH_LED1
- J3 pad 24: GPIO26 -> RPI_GPIO26
- J3 pad 25: GPIO21 -> RPI_GPIO21
- J3 pad 26: GPIO19 -> RPI_GPIO19
- J3 pad 27: GPIO20 -> RPI_GPIO20
- J3 pad 28: GPIO13 -> RPI_GPIO13
- J3 pad 29: GPIO16 -> RPI_GPIO16
- J3 pad 3: TRD3_P -> ETH3_P
- J3 pad 30: GPIO6 -> RPI_GPIO6
- J3 pad 31: GPIO12 -> RPI_GPIO12
- J3 pad 34: GPIO5 -> RPI_GPIO5
- J3 pad 35: ID_SC -> RPI_ID_SC
- J3 pad 36: ID_SD -> RPI_ID_SD
- J3 pad 37: GPIO7 -> RPI_GPIO7
- J3 pad 38: GPIO11 -> RPI_GPIO11
- J3 pad 39: GPIO8 -> RPI_GPIO8
- J3 pad 4: TRD1_P -> ETH1_P
- J3 pad 40: GPIO9 -> RPI_GPIO9
- J3 pad 41: GPIO25 -> RPI_GPIO25
- J3 pad 44: GPIO10 -> RPI_GPIO10
- J3 pad 45: GPIO24 -> RPI_GPIO24
- J3 pad 46: GPIO22 -> RPI_GPIO22
- J3 pad 47: GPIO23 -> RPI_GPIO23
- J3 pad 48: GPIO27 -> RPI_GPIO27
- J3 pad 49: GPIO18 -> RPI_GPIO18
- J3 pad 5: TRD3_N -> ETH3_N
- J3 pad 50: GPIO17 -> RPI_GPIO17
- J3 pad 51: GPIO15 -> RPI_GPIO15
- J3 pad 54: GPIO4 -> RPI_GPIO4
- J3 pad 55: GPIO14 -> RPI_GPIO14
- J3 pad 56: GPIO3 -> RPI_GPIO3
- J3 pad 57: SD_CLK -> SDIO0_CLK
- J3 pad 58: GPIO2 -> RPI_GPIO2
- J3 pad 6: TRD1_N -> ETH1_N
- J3 pad 61: SD_DAT3 -> SDIO0_D3
- J3 pad 62: SD_CMD -> SDIO0_CMD
- J3 pad 63: SD_DAT0 -> SDIO0_D0
- J3 pad 67: SD_DAT1 -> SDIO0_D1
- J3 pad 69: SD_DAT2 -> SDIO0_D2
- J3 pad 79: Net-(J3-Pad79) -> 5V0_IN
- J3 pad 80: SCL0 -> I2C0_SCL
- J3 pad 81: Net-(J3-Pad81) -> 5V0_IN
- J3 pad 82: SDA0 -> I2C0_SDA
- J3 pad 83: Net-(J3-Pad83) -> 5V0_IN
- J3 pad 85: Net-(J3-Pad85) -> 5V0_IN
- J3 pad 87: Net-(J3-Pad85) -> 5V0_IN
- J3 pad 9: TRD2_N -> ETH2_N
- J4 pad 100: HDMI0_SCL -> HDMI_DSCL
- J4 pad 15: CAM1_D0_N -> CSI2RX_D0_N
- J4 pad 17: CAM1_D0_P -> CSI2RX_D0_P
- J4 pad 21: CAM1_D1_N -> CSI2RX_D1_N
- J4 pad 23: CAM1_D1_P -> CSI2RX_D1_P
- J4 pad 27: CAM1_C_N -> CSI2RX_CLK_N
- J4 pad 28: CAM0_D0_N -> CSI1RX_D0_N
- J4 pad 29: CAM1_C_P -> CSI2RX_CLK_P
- J4 pad 3: USB2_N -> USBDM_N
- J4 pad 30: CAM0_D0_P -> CSI1RX_D0_P
- J4 pad 34: CAM0_D1_N -> CSI1RX_D1_N
- J4 pad 36: CAM0_D1_P -> CSI1RX_D1_P
- J4 pad 40: CAM0_C_N -> CSI1RX_CLK_N
- J4 pad 42: CAM0_C_P -> CSI1RX_CLK_P
- J4 pad 5: USB2_P -> USBDP_P
- J4 pad 51: HDMI0_CEC -> HDMI_CEC
- J4 pad 53: HDMI0_HOTPLUG -> HDMI_HPD
- J4 pad 70: HDMI0_D2_P -> HDMI_TX2_P
- J4 pad 72: HDMI0_D2_N -> HDMI_TX2_N
- J4 pad 76: HDMI0_D1_P -> HDMI_TX1_P
- J4 pad 78: HDMI0_D1_N -> HDMI_TX1_N
- J4 pad 82: HDMI0_D0_P -> HDMI_TX0_P
- J4 pad 84: HDMI0_D0_N -> HDMI_TX0_N
- J4 pad 88: HDMI0_CK_P -> HDMI_TXC_P
- J4 pad 90: HDMI0_CK_N -> HDMI_TXC_N
- J4 pad 99: HDMI0_SDA -> HDMI_DSDA
- U11 pad 10: /Ethernet/ETH3_P -> ETH3_P
- U11 pad 11: /Ethernet/ETH3_N -> ETH3_N
- U11 pad 15: /Ethernet/ETH_LED2 -> ETH_LED2
- U11 pad 17: /Ethernet/ETH_LED1 -> ETH_LED1
- U11 pad 2: /Ethernet/ETH0_P -> ETH0_P
- U11 pad 3: /Ethernet/ETH0_N -> ETH0_N
- U11 pad 5: /Ethernet/ETH1_P -> ETH1_P
- U11 pad 6: /Ethernet/ETH1_N -> ETH1_N
- U11 pad 7: /Ethernet/ETH2_P -> ETH2_P
- U11 pad 8: /Ethernet/ETH2_N -> ETH2_N
- U13 pad AA1: Net-(R62-Pad2) -> LCD_VSYNC
- U13 pad AA2: Net-(R67-Pad2) -> LCD_DATA3
- U13 pad AA25: GMAC_TXD2 -> RGMII_TXD2
- U13 pad AA26: GMAC_TXD1 -> RGMII_TXD1
- U13 pad AA27: GMAC_GTXCLK -> RGMII_TX_CLK
- U13 pad AA3: Net-(R60-Pad2) -> LCD_PCLK
- U13 pad AA31: GMAC_RXDV -> RGMII_RX_DV
- U13 pad AA4: Net-(R61-Pad2) -> LCD_DE
- U13 pad AA5: Net-(R64-Pad2) -> LCD_DATA0
- U13 pad AA6: Net-(R65-Pad2) -> LCD_DATA1
- U13 pad AB1: Net-(R66-Pad2) -> LCD_DATA2
- U13 pad AB2: Net-(R71-Pad2) -> LCD_DATA7
- U13 pad AB31: GMAC_TXD0 -> RGMII_TXD0
- U13 pad AB4: Net-(R75-Pad2) -> LCD_DATA11
- U13 pad AB5: Net-(R68-Pad2) -> LCD_DATA4
- U13 pad AB6: Net-(R69-Pad2) -> LCD_DATA5
- U13 pad AB7: Net-(R72-Pad2) -> LCD_DATA8
- U13 pad AC1: Net-(R70-Pad2) -> LCD_DATA6
- U13 pad AD1: Net-(R74-Pad2) -> LCD_DATA10
- U13 pad AD2: Net-(R79-Pad2) -> LCD_DATA15
- U13 pad AD3: Net-(R82-Pad2) -> LCD_DATA18
- U13 pad AD4: Net-(R86-Pad2) -> LCD_DATA22
- U13 pad AD5: Net-(R87-Pad2) -> LCD_DATA23
- U13 pad AE1: Net-(R78-Pad2) -> LCD_DATA14
- U13 pad AE2: Net-(R83-Pad2) -> LCD_DATA19
- U13 pad AE4: Net-(R84-Pad2) -> LCD_DATA20
- U13 pad AG2: Net-(R73-Pad2) -> LCD_DATA9
- U13 pad AG3: Net-(R77-Pad2) -> LCD_DATA13
- U13 pad AG4: Net-(R81-Pad2) -> LCD_DATA17
- U13 pad AL3: Net-(R80-Pad2) -> LCD_DATA16
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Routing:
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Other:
- board text added: "CAM1"
- board text added: "CAM2"
- board text added: "CSI&DSI"
- board text added: "DDR0"
- board text added: "DDR1"
- board text added: "DSI"
- board text added: "ETH"
- board text added: "GPIO"
- board text added: "HDMI"
- board text added: "LCD"
- board text added: "QSPI"
- board text added: "RGMII"
- board text added: "SDIO"
- board text added: "USB"
